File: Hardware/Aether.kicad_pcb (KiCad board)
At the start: 2 copper layers, 67.5 x 27 mm, 78 parts, among them J1 PRGM, J2 CONN-2, J3 CONN-2, J4 CONN-2, J5 CONN-2, J6 CONN-3, J7 CONN-3, Q1 IRLML6401, U1 ANTENOVA-UB, U2 ADF7012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

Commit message: Majority of layout
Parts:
- moved C31 2.00 mm to (162.0, 96.5)
- moved C33 2.00 mm to (164.5, 96.5)
- moved X2 2.00 mm to (163.2, 99.0)
- moved C24 1.00 mm to (139.8, 96.5)
- moved C28 1.00 mm to (138.5, 105.5)
- moved C29 1.00 mm to (139.8, 107.5)
- moved L8 1.00 mm to (139.8, 99.2)
- moved R9 1.00 mm to (141.0, 105.5)
- moved U3 1.00 mm to (139.8, 103.0)
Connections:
- J3 pad 1: (no net) -> /Core/E2
- J3 pad 2: (no net) -> /Core/E1
- U5 pad 18: (no net) -> /Core/E2
- U5 pad 19: (no net) -> /Core/E1
- U5 pad 20: (no net) -> /Core/GPS_En
- U5 pad 6: (no net) -> /Core/GPS_Perf
- U5 pad 7: /Core/GPS_Perf -> (no net)
- U5 pad 8: /Core/GPS_En -> (no net)
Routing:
- net +3.3V: track 36.1 -> 107.4 mm, vias 1 -> 2
- net +BATT: track 0.00 -> 61.1 mm, vias 0 -> 1
- net /Core/RX: track 28.7 -> 0.00 mm, vias 2 -> 0
- net /Core/GPS_En: track 1.60 -> 24.7 mm, vias 0 -> 2
- net /GPS/RX: track 22.9 -> 0.00 mm, vias 2 -> 0
- net /Core/E2: track 0.00 -> 20.7 mm, vias 0 -> 1
- net /Core/E1: track 0.00 -> 18.5 mm, vias 0 -> 1
- net /Core/SDA: track 0.00 -> 12.9 mm
- net /Core/SCL: track 0.00 -> 11.0 mm
- net GND: track 100.8 -> 110.5 mm, vias 28 -> 38
- net +5V: track 4.14 -> 0.00 mm, vias 1 -> 0
- net /Core/CLK_En: track 19.3 -> 22.8 mm
- net /Core/XOut: track 9.03 -> 11.0 mm
- net /Core/XIn: track 9.03 -> 11.0 mm
- net N-0000064: track 0.00 -> 1.74 mm
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- added copper zone on F.Cu, net +3.3V
- added copper zone on F.Cu, net +BATT
- added copper zone on F.Cu, net /Core/Lx
- added copper zone on F.Cu, net GND
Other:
- board size 67.5 x 27 mm -> 66.5 x 26 mm

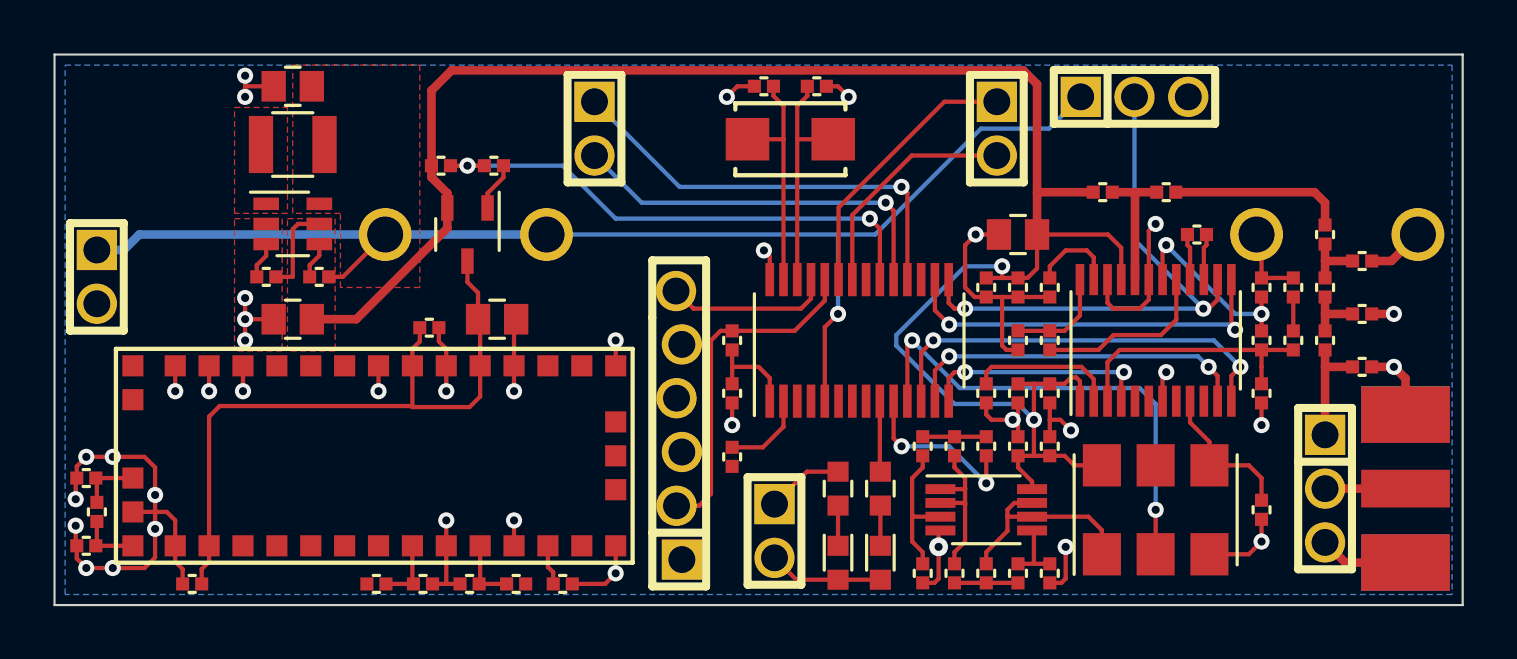
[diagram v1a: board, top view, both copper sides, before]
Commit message: Add fiducials and mount holes
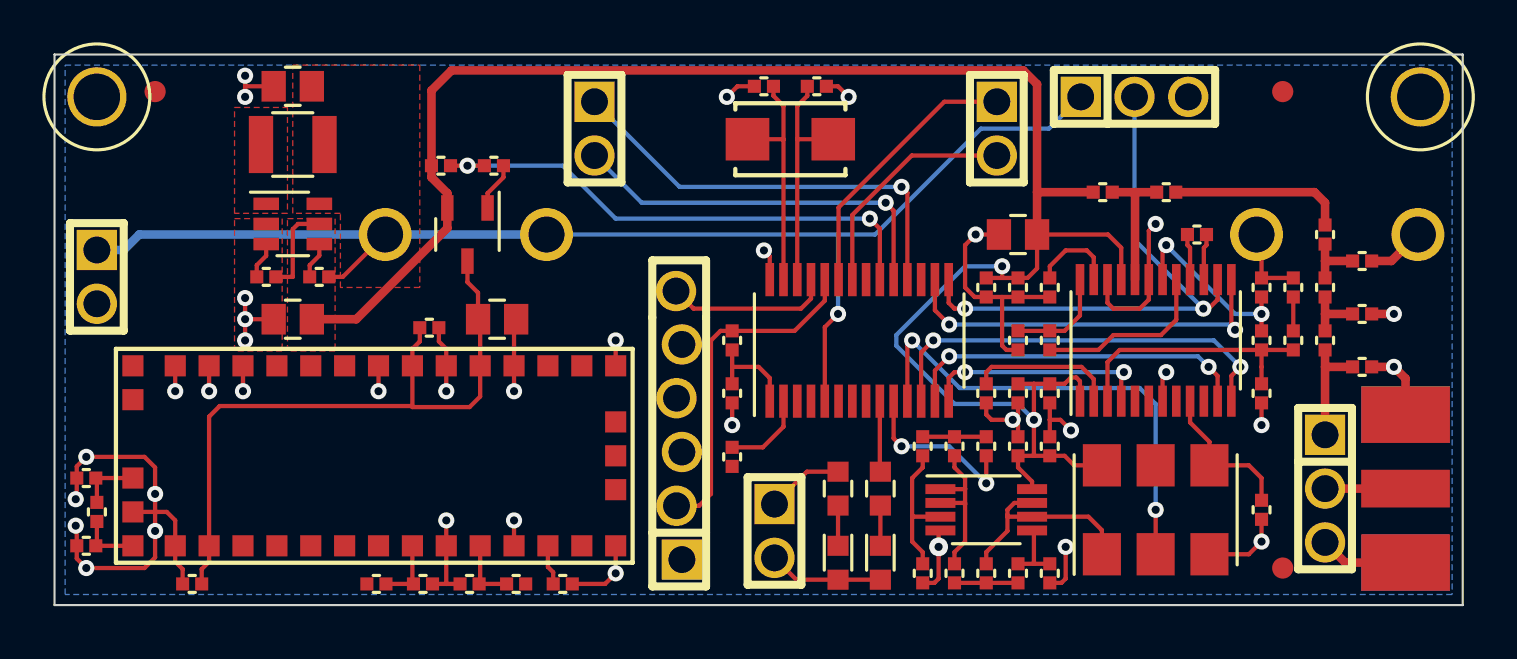
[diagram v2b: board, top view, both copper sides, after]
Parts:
- added FIDUCIAL-1MM: VAL**, FIDUCIAL-1MM, F.Cu at (133.2, 96.8)
- added FIDUCIAL-1MM: VAL**, FIDUCIAL-1MM, F.Cu at (186.5, 96.8)
- added FIDUCIAL-1MM: VAL**, FIDUCIAL-1MM, F.Cu at (186.5, 119.2)
- added MECH-HOLE220: VAL**, MECH-HOLE220, F.Cu at (130.5, 97.0)
- added MECH-HOLE220: VAL**, MECH-HOLE220, F.Cu at (193.0, 97.0)
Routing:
- net GND: vias 38 -> 36
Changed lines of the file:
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@@
 (kicad_pcb (version 3) (host pcbnew "(2013-07-07 BZR 4022)-stable")
   (general
-    (links 182)
-    (no_connects 10)
-    (area 126.8424 93.0644 207.293981 122.9356)
+    (links 0)
+    (no_connects 9)
+    (area 123.555134 93.0644 207.293981 122.9356)
     (thickness 1.6)
     (drawings 4)
-    (tracks 482)
+    (tracks 479)
     (zones 0)
-    (modules 78)
+    (modules 83)
     (nets 59)
   )
@@
     )
   )
+  (module MECH-HOLE220 (layer F.Cu)
+    (at 130.5 97)
+    (fp_text reference MECH-HOLE220 (at 0 0) (layer F.SilkS) hide
+      (effects (font (size 1 1) (thickness 0.15)))
+    )
+    (fp_text value VAL** (at 0 0) (layer F.SilkS) hide
+      (effects (font (size 1 1) (thickness 0.15)))
+    )
+    (fp_circle (center 0 0) (end 2.5 0) (layer F.SilkS) (width 0.15))
+    (pad "" thru_hole circle (at 0 0) (size 2.8 2.8) (drill 2.2)
+      (layers *.Cu *.Mask F.SilkS)
+    )
+  )
+  (module FIDUCIAL-1MM (layer F.Cu)
+    (at 133.25 96.75)
+    (fp_text reference FIDUCIAL-1MM (at 0 -1.5) (layer F.SilkS) hide
+      (effects (font (size 1 1) (thickness 0.15)))
+    )
+    (fp_text value VAL** (at 0 1.5) (layer F.SilkS) hide
+      (effects (font (size 1 1) (thickness 0.15)))
+    )
+    (pad "" smd circle (at 0 0 90) (size 1 1)
+      (layers F.Cu F.Mask)
+      (solder_mask_margin 0.5)
+      (clearance 0.5)
+    )
+  )
+  (module MECH-HOLE220 (layer F.Cu)
+    (at 193 97)
+    (fp_text reference MECH-HOLE220 (at 0 0) (layer F.SilkS) hide
+      (effects (font (size 1 1) (thickness 0.15)))
+    )
+    (fp_text value VAL** (at 0 0) (layer F.SilkS) hide
+      (effects (font (size 1 1) (thickness 0.15)))
+    )
+    (fp_circle (center 0 0) (end 2.5 0) (layer F.SilkS) (width 0.15))
+    (pad "" thru_hole circle (at 0 0) (size 2.8 2.8) (drill 2.2)
+      (layers *.Cu *.Mask F.SilkS)
+    )
+  )
+  (module FIDUCIAL-1MM (layer F.Cu)
+    (at 186.5 96.75)
+    (fp_text reference FIDUCIAL-1MM (at 0 -1.5) (layer F.SilkS) hide
+      (effects (font (size 1 1) (thickness 0.15)))
+    )
+    (fp_text value VAL** (at 0 1.5) (layer F.SilkS) hide
+      (effects (font (size 1 1) (thickness 0.15)))
+    )
+    (pad "" smd circle (at 0 0 90) (size 1 1)
+      (layers F.Cu F.Mask)
+      (solder_mask_margin 0.5)
+      (clearance 0.5)
+    )
+  )
+  (module FIDUCIAL-1MM (layer F.Cu)
+    (at 186.5 119.25)
+    (fp_text reference FIDUCIAL-1MM (at 0 -1.5) (layer F.SilkS) hide
+      (effects (font (size 1 1) (thickness 0.15)))
+    )
+    (fp_text value VAL** (at 0 1.5) (layer F.SilkS) hide
+      (effects (font (size 1 1) (thickness 0.15)))
+    )
+    (pad "" smd circle (at 0 0 90) (size 1 1)
+      (layers F.Cu F.Mask)
+      (solder_mask_margin 0.5)
+      (clearance 0.5)
+    )
+  )
   (gr_line (start 128.5 95) (end 128.5 121) (angle 90) (layer Edge.Cuts) (width 0.1))
   (gr_line (start 195 95) (end 128.5 95) (angle 90) (layer Edge.Cuts) (width 0.1))
@@
   (segment (start 185.5 108.05) (end 185.5 107.25) (width 0.2032) (layer F.Cu) (net 31))
   (segment (start 185.5 107.25) (end 185.5 106.45) (width 0.2032) (layer F.Cu) (net 31))
+  (segment (start 130 114) (end 132.75 114) (width 0.2032) (layer F.Cu) (net 32))
+  (via (at 133.25 115.75) (size 0.762) (layers F.Cu B.Cu) (net 32))
+  (segment (start 133.25 116.6) (end 133.25 115.75) (width 0.2032) (layer F.Cu) (net 32))
+  (segment (start 129.55 114.45) (end 130 114) (width 0.2032) (layer F.Cu) (net 32))
+  (via (at 130 114) (size 0.762) (layers F.Cu B.Cu) (net 32))
+  (segment (start 129.55 114.45) (end 129.55 115) (width 0.2032) (layer F.Cu) (net 32))
+  (segment (start 133.25 114.5) (end 133.25 115.75) (width 0.2032) (layer F.Cu) (net 32))
+  (segment (start 132.75 114) (end 133.25 114.5) (width 0.2032) (layer F.Cu) (net 32))
+  (segment (start 130 119.25) (end 132.75 119.25) (width 0.2032) (layer F.Cu) (net 32))
+  (via (at 133.25 117.5) (size 0.762) (layers F.Cu B.Cu) (net 32))
+  (segment (start 133.25 116.6) (end 133.25 117.5) (width 0.2032) (layer F.Cu) (net 32))
+  (segment (start 129.55 118.8) (end 130 119.25) (width 0.2032) (layer F.Cu) (net 32))
+  (via (at 130 119.25) (size 0.762) (layers F.Cu B.Cu) (net 32))
+  (segment (start 129.55 118.8) (end 129.55 118.2) (width 0.2032) (layer F.Cu) (net 32))
+  (segment (start 133.25 118.75) (end 133.25 117.5) (width 0.2032) (layer F.Cu) (net 32))
+  (segment (start 132.75 119.25) (end 133.25 118.75) (width 0.2032) (layer F.Cu) (net 32))
+  (segment (start 129.55 115) (end 129.55 115.95) (width 0.2032) (layer F.Cu) (net 32))
+  (segment (start 129.55 115.95) (end 129.5 116) (width 0.2032) (layer F.Cu) (net 32))
+  (via (at 129.5 116) (size 0.762) (layers F.Cu B.Cu) (net 32))
+  (segment (start 129.55 118.2) (end 129.55 117.3) (width 0.2032) (layer F.Cu) (net 32))
+  (segment (start 129.55 117.3) (end 129.5 117.25) (width 0.2032) (layer F.Cu) (net 32))
+  (via (at 129.5 117.25) (size 0.762) (layers F.Cu B.Cu) (net 32))
   (via (at 155 119.5) (size 0.762) (layers F.Cu B.Cu) (net 32))
   (segment (start 175.5 119.95) (end 176.05 119.95) (width 0.2032) (layer F.Cu) (net 32))
@@
   (segment (start 147 109.7) (end 147 110.9) (width 0.2032) (layer F.Cu) (net 32))
   (via (at 147 110.9) (size 0.762) (layers F.Cu B.Cu) (net 32))
-  (via (at 133.25 117.4) (size 0.762) (layers F.Cu B.Cu) (net 32))
-  (via (at 133.25 115.8) (size 0.762) (layers F.Cu B.Cu) (net 32))
-  (via (at 131.25 114) (size 0.762) (layers F.Cu B.Cu) (net 32))
-  (via (at 131.25 119.25) (size 0.762) (layers F.Cu B.Cu) (net 32))
   (segment (start 147 109.7) (end 147 108.9) (width 0.2032) (layer F.Cu) (net 32))
   (segment (start 146.65 108.55) (end 146.65 107.9) (width 0.2032) (layer F.Cu) (net 32))
@@
   (segment (start 146.35 120) (end 147 120) (width 0.2032) (layer F.Cu) (net 32))
   (segment (start 147 120) (end 147.65 120) (width 0.2032) (layer F.Cu) (net 32))
-  (segment (start 130 119.25) (end 131.25 119.25) (width 0.2032) (layer F.Cu) (net 32))
-  (segment (start 131.25 119.25) (end 132.75 119.25) (width 0.2032) (layer F.Cu) (net 32))
-  (segment (start 132.75 119.25) (end 133.25 118.75) (width 0.2032) (layer F.Cu) (net 32))
-  (segment (start 133.25 118.75) (end 133.25 117.4) (width 0.2032) (layer F.Cu) (net 32))
-  (segment (start 133.25 117.4) (end 133.25 115.8) (width 0.2032) (layer F.Cu) (net 32))
-  (segment (start 133.25 115.8) (end 133.25 114.5) (width 0.2032) (layer F.Cu) (net 32))
-  (segment (start 133.25 114.5) (end 132.75 114) (width 0.2032) (layer F.Cu) (net 32))
-  (segment (start 132.75 114) (end 131.25 114) (width 0.2032) (layer F.Cu) (net 32))
-  (segment (start 131.25 114) (end 130 114) (width 0.2032) (layer F.Cu) (net 32))
-  (segment (start 129.55 114.45) (end 130 114) (width 0.2032) (layer F.Cu) (net 32))
-  (via (at 130 114) (size 0.762) (layers F.Cu B.Cu) (net 32))
-  (segment (start 129.55 114.45) (end 129.55 115) (width 0.2032) (layer F.Cu) (net 32))
-  (segment (start 129.55 118.2) (end 129.55 118.8) (width 0.2032) (layer F.Cu) (net 32))
-  (via (at 130 119.25) (size 0.762) (layers F.Cu B.Cu) (net 32))
-  (segment (start 129.55 118.8) (end 130 119.25) (width 0.2032) (layer F.Cu) (net 32))
-  (segment (start 129.5 115.05) (end 129.5 116) (width 0.2032) (layer F.Cu) (net 32))
-  (via (at 129.5 116) (size 0.762) (layers F.Cu B.Cu) (net 32))
-  (segment (start 129.55 115) (end 129.5 115.05) (width 0.2032) (layer F.Cu) (net 32))
-  (segment (start 129.5 118.15) (end 129.5 117.25) (width 0.2032) (layer F.Cu) (net 32))
-  (via (at 129.5 117.25) (size 0.762) (layers F.Cu B.Cu) (net 32))
-  (segment (start 129.5 118.15) (end 129.55 118.2) (width 0.2032) (layer F.Cu) (net 32))
   (segment (start 134.2 118.2) (end 134.2 118.95) (width 0.2032) (layer F.Cu) (net 32))
   (segment (start 134.2 118.95) (end 134.55 119.3) (width 0.2032) (layer F.Cu) (net 32))
